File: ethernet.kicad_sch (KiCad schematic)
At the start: 39 parts, among them J1001 7499010121A, U1001 LAN8742A-CZ-TR, U1002 USBLC6-4SC6

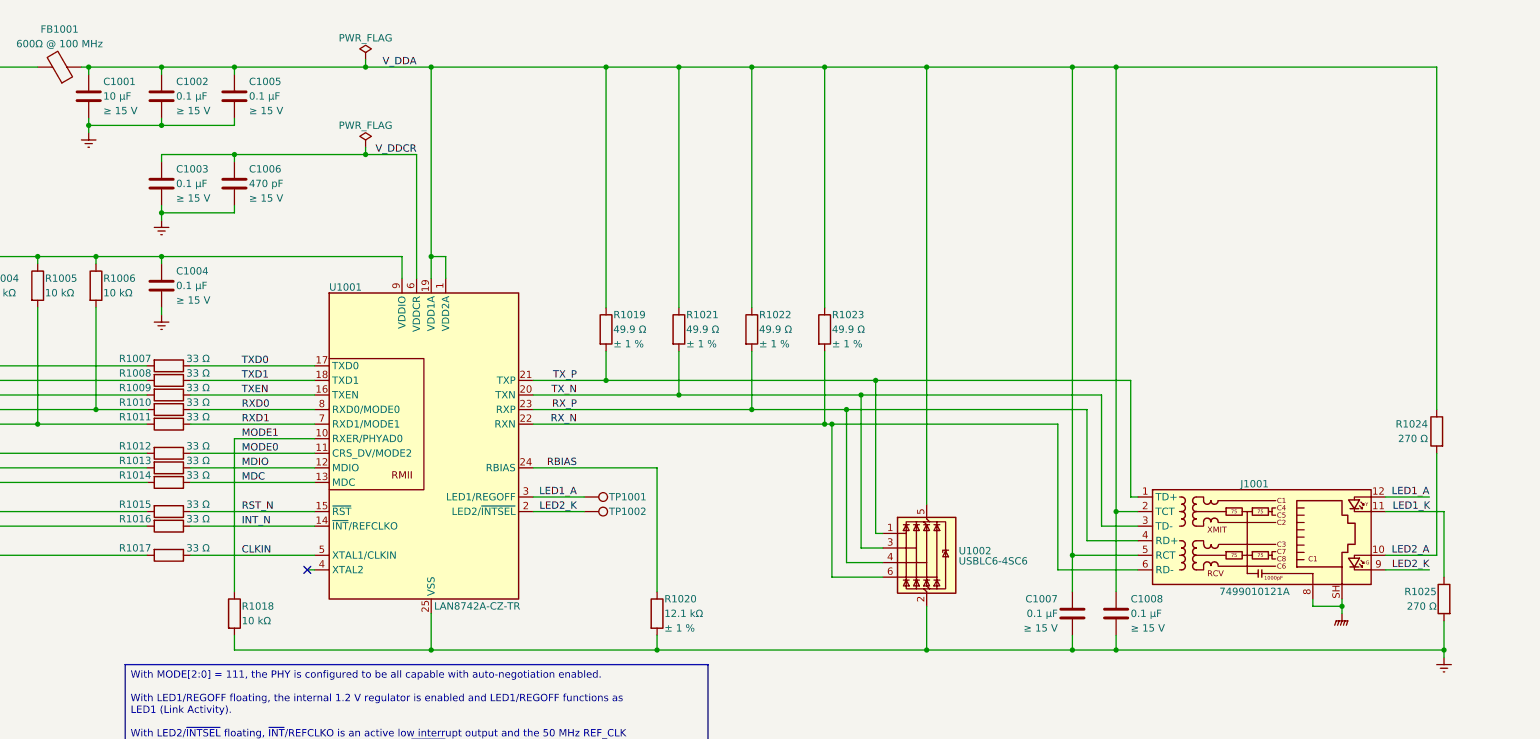
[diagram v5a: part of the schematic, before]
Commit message: Fix component values
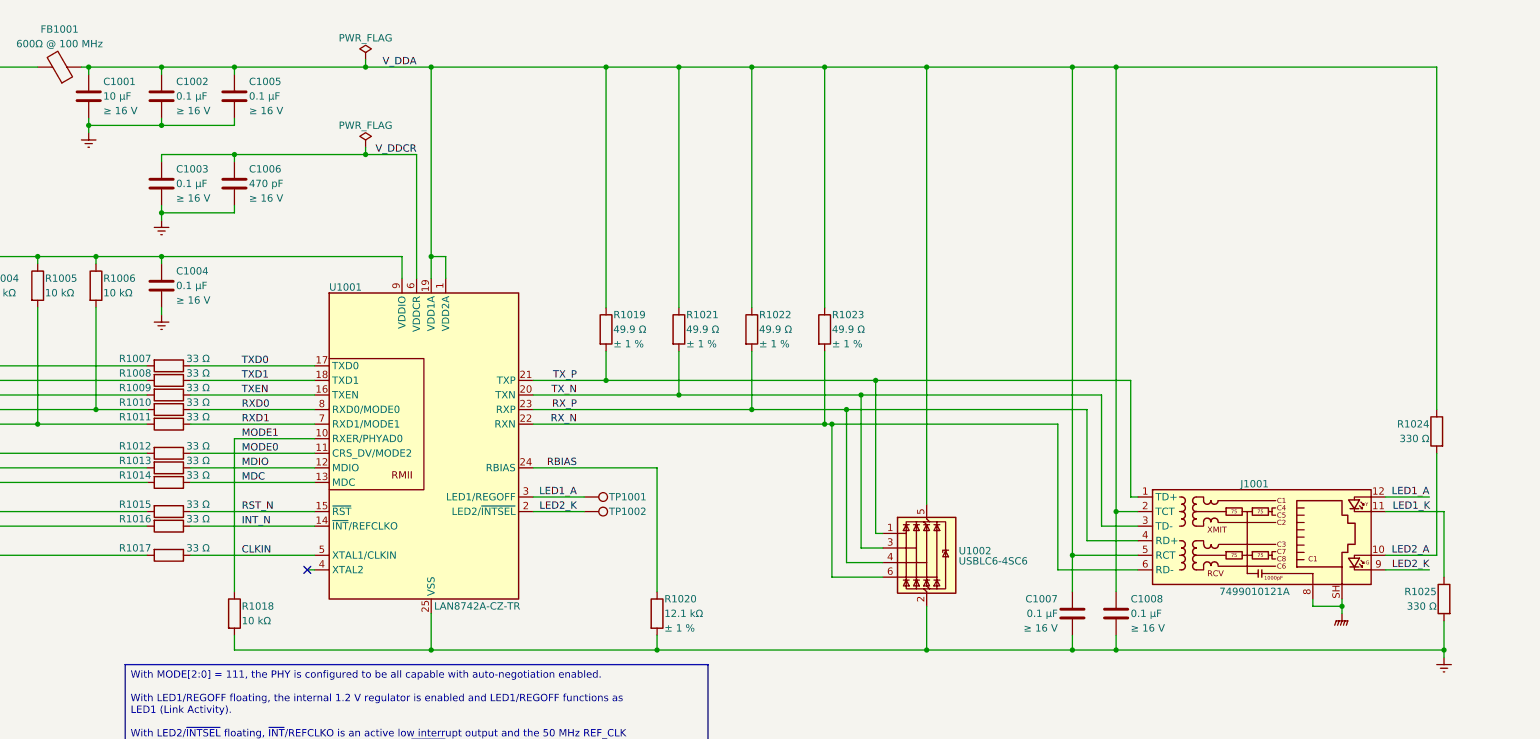
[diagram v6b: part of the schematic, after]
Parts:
- C1001, C1002, C1003, C1004, C1005, C1006, C1007, C1008: Voltage rating ≥ 15 V -> ≥ 16 V
- R1024, R1025: value 270 Ω -> 330 Ω; MPN (none) -> 560112110019; Manufacturer (none) -> Würth Elektronik
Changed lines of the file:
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@@
 			)
 		)
-		(property "Voltage rating" "≥ 15 V"
+		(property "Voltage rating" "≥ 16 V"
 			(at 135.89 140.9701 0)
 			(effects
@@
 			)
 		)
-		(property "Voltage rating" "≥ 15 V"
+		(property "Voltage rating" "≥ 16 V"
 			(at 289.56 215.9001 0)
 			(effects
@@
 			)
 		)
-		(property "Voltage rating" "≥ 15 V"
+		(property "Voltage rating" "≥ 16 V"
 			(at 148.59 125.7301 0)
 			(effects
@@
 	)
 	(symbol
-		(lib_id "Device:R")
-		(at 355.6 181.61 0)
-		(mirror y)
-		(unit 1)
-		(exclude_from_sim no)
-		(in_bom yes)
-		(on_board yes)
-		(dnp no)
-		(property "Reference" "R1024"
-			(at 354.076 180.34 0)
-			(effects
-				(font
-					(size 1.27 1.27)
-				)
-				(justify left)
-			)
-		)
-		(property "Value" "270 Ω"
-			(at 354.076 182.88 0)
-			(effects
-				(font
-					(size 1.27 1.27)
-				)
-				(justify left)
-			)
-		)
-		(property "Footprint" "perfect_footprints:R_0402_1005Metric"
-			(at 357.378 181.61 90)
-			(effects
-				(font
-					(size 1.27 1.27)
-				)
-				(hide yes)
-			)
-		)
-		(property "Datasheet" ""
-			(at 355.6 181.61 0)
-			(effects
-				(font
-					(size 1.27 1.27)
-				)
-				(hide yes)
-			)
-		)
-		(property "Description" "Resistor"
-			(at 355.6 181.61 0)
-			(effects
-				(font
-					(size 1.27 1.27)
-				)
-				(hide yes)
-			)
-		)
-		(property "MPN" ""
-			(at 355.6 181.61 0)
-			(effects
-				(font
-					(size 1.27 1.27)
-				)
-				(hide yes)
-			)
-		)
-		(property "Manufacturer" ""
-			(at 355.6 181.61 0)
-			(effects
-				(font
-					(size 1.27 1.27)
-				)
-				(hide yes)
-			)
-		)
-		(pin "2"
-		)
-		(pin "1"
-		)
-		(instances
-			(project "linux-sbc"
-				(path "/fa11a02f-8043-4153-ab69-88d766503017/9ca4e50e-b0f6-43cd-b87d-1fd05ae8a1fe"
-					(reference "R1024")
-					(unit 1)
-				)
-			)
-		)
-	)
-	(symbol
 		(lib_id "Power_Protection:USBLC6-4SC6")
 		(at 266.7 201.93 0)
@@
 			)
 		)
-		(property "Voltage rating" "≥ 15 V"
+		(property "Voltage rating" "≥ 16 V"
 			(at 123.19 125.7301 0)
 			(effects
@@
 			)
 		)
-		(property "Voltage rating" "≥ 15 V"
+		(property "Voltage rating" "≥ 16 V"
 			(at 135.89 158.7501 0)
 			(effects
@@
 			)
 		)
-		(property "Voltage rating" "≥ 15 V"
+		(property "Voltage rating" "≥ 16 V"
 			(at 148.59 140.9701 0)
 			(effects
@@
 	)
 	(symbol
+		(lib_id "Device:R")
+		(at 356.87 210.82 0)
+		(mirror y)
+		(unit 1)
+		(exclude_from_sim no)
+		(in_bom yes)
+		(on_board yes)
+		(dnp no)
+		(property "Reference" "R1025"
+			(at 355.6 209.55 0)
+			(effects
+				(font
+					(size 1.27 1.27)
+				)
+				(justify left)
+			)
+		)
+		(property "Value" "330 Ω"
+			(at 355.6 212.09 0)
+			(effects
+				(font
+					(size 1.27 1.27)
+				)
+				(justify left)
+			)
+		)
+		(property "Footprint" "perfect_footprints:R_0402_1005Metric"
+			(at 358.648 210.82 90)
+			(effects
+				(font
+					(size 1.27 1.27)
+				)
+				(hide yes)
+			)
+		)
+		(property "Datasheet" "https://www.we-online.com/components/products/datasheet/560112110019.pdf"
+			(at 356.87 210.82 0)
+			(effects
+				(font
+					(size 1.27 1.27)
+				)
+				(hide yes)
+			)
+		)
+		(property "Description" "Resistor"
+			(at 356.87 210.82 0)
+			(effects
+				(font
+					(size 1.27 1.27)
+				)
+				(hide yes)
+			)
+		)
+		(property "MPN" "560112110019"
+			(at 356.87 210.82 0)
+			(effects
+				(font
+					(size 1.27 1.27)
+				)
+				(hide yes)
+			)
+		)
+		(property "Manufacturer" "Würth Elektronik"
+			(at 356.87 210.82 0)
+			(effects
+				(font
+					(size 1.27 1.27)
+				)
+				(hide yes)
+			)
+		)
+		(pin "2"
+		)
+		(pin "1"
+		)
+		(instances
+			(project "linux-sbc"
+				(path "/fa11a02f-8043-4153-ab69-88d766503017/9ca4e50e-b0f6-43cd-b87d-1fd05ae8a1fe"
+					(reference "R1025")
+					(unit 1)
+				)
+			)
+		)
+	)
+	(symbol
 		(lib_id "Interface_Ethernet:LAN8742A")
 		(at 180.34 185.42 0)
@@
 	)
 	(symbol
-		(lib_id "Device:C")
-		(at 133.35 123.19 0)
+		(lib_id "Device:R")
+		(at 355.6 181.61 0)
+		(mirror y)
 		(unit 1)
 		(exclude_from_sim no)
@@
 		(on_board yes)
 		(dnp no)
-		(property "Reference" "C1002"
-			(at 135.89 120.65 0)
+		(property "Reference" "R1024"
+			(at 354.33 180.34 0)
 			(effects
 				(font
@@
 			)
 		)
-		(property "Value" "0.1 µF"
-			(at 135.89 123.19 0)
+		(property "Value" "330 Ω"
+			(at 354.33 182.88 0)
 			(effects
 				(font
@@
 			)
 		)
-		(property "Footprint" ""
-			(at 134.3152 127 0)
+		(property "Footprint" "perfect_footprints:R_0402_1005Metric"
+			(at 357.378 181.61 90)
 			(effects
 				(font
@@
 			)
 		)
-		(property "Datasheet" ""
-			(at 133.35 123.19 0)
+		(property "Datasheet" "https://www.we-online.com/components/products/datasheet/560112110019.pdf"
+			(at 355.6 181.61 0)
 			(effects
 				(font
@@
 			)
 		)
-		(property "Description" ""
-			(at 133.35 123.19 0)
+		(property "Description" "Resistor"
+			(at 355.6 181.61 0)
 			(effects
 				(font
@@
 			)
 		)
-		(property "MPN" ""
-			(at 133.35 123.19 0)
+		(property "MPN" "560112110019"
+			(at 355.6 181.61 0)
 			(effects
 				(font
@@
 			)
 		)
-		(property "Manufacturer" ""
-			(at 133.35 123.19 0)
+		(property "Manufacturer" "Würth Elektronik"
+			(at 355.6 181.61 0)
 			(effects
 				(font
@@
 			)
 		)
-		(property "Voltage rating" "≥ 15 V"
-			(at 135.89 125.7301 0)
-			(effects
-				(font
-					(size 1.27 1.27)
-				)
-				(justify left)
-			)
-		)
 		(pin "2"
 		)
@@
 			(project "linux-sbc"
 				(path "/fa11a02f-8043-4153-ab69-88d766503017/9ca4e50e-b0f6-43cd-b87d-1fd05ae8a1fe"
-					(reference "C1002")
+					(reference "R1024")
 					(unit 1)
 				)
@@
 	)
 	(symbol
-		(lib_id "Device:R")
-		(at 356.87 210.82 0)
-		(mirror y)
+		(lib_id "Device:C")
+		(at 133.35 123.19 0)
 		(unit 1)
 		(exclude_from_sim no)
@@
 		(on_board yes)
 		(dnp no)
-		(property "Reference" "R1025"
-			(at 355.6 209.55 0)
+		(property "Reference" "C1002"
+			(at 135.89 120.65 0)
 			(effects
 				(font
@@
 			)
 		)
-		(property "Value" "270 Ω"
-			(at 355.6 212.09 0)
+		(property "Value" "0.1 µF"
+			(at 135.89 123.19 0)
 			(effects
 				(font
@@
 			)
 		)
-		(property "Footprint" "perfect_footprints:R_0402_1005Metric"
-			(at 358.648 210.82 90)
+		(property "Footprint" ""
+			(at 134.3152 127 0)
 			(effects
 				(font
@@
 		)
 		(property "Datasheet" ""
-			(at 356.87 210.82 0)
+			(at 133.35 123.19 0)
 			(effects
 				(font
@@
 			)
 		)
-		(property "Description" "Resistor"
-			(at 356.87 210.82 0)
+		(property "Description" ""
+			(at 133.35 123.19 0)
 			(effects
 				(font
@@
 		)
 		(property "MPN" ""
-			(at 356.87 210.82 0)
+			(at 133.35 123.19 0)
 			(effects
 				(font
@@
 		)
 		(property "Manufacturer" ""
-			(at 356.87 210.82 0)
+			(at 133.35 123.19 0)
 			(effects
 				(font
@@
 			)
 		)
+		(property "Voltage rating" "≥ 16 V"
+			(at 135.89 125.7301 0)
+			(effects
+				(font
+					(size 1.27 1.27)
+				)
+				(justify left)
+			)
+		)
 		(pin "2"
 		)
@@
 			(project "linux-sbc"
 				(path "/fa11a02f-8043-4153-ab69-88d766503017/9ca4e50e-b0f6-43cd-b87d-1fd05ae8a1fe"
-					(reference "R1025")
+					(reference "C1002")
 					(unit 1)
 				)
@@
 			)
 		)
-		(property "Voltage rating" "≥ 15 V"
+		(property "Voltage rating" "≥ 16 V"
 			(at 302.26 215.9001 0)
 			(effects

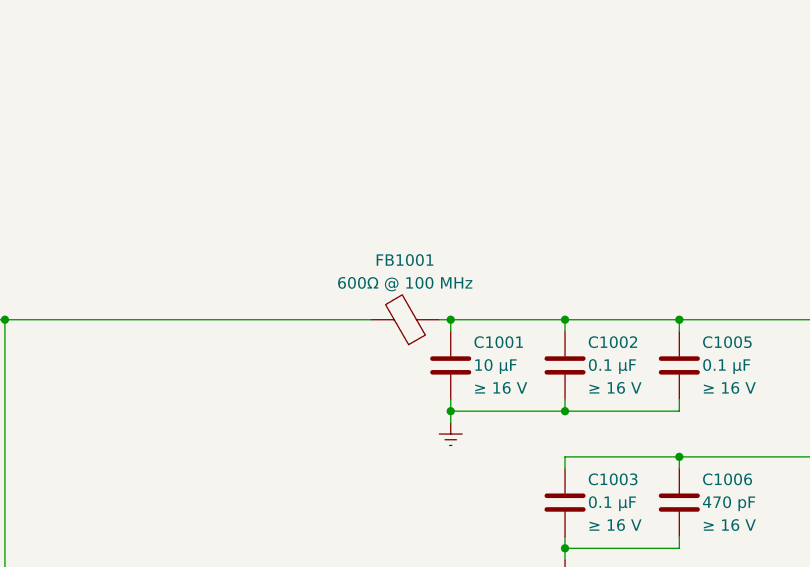
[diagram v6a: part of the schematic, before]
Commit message: Refactor schematics
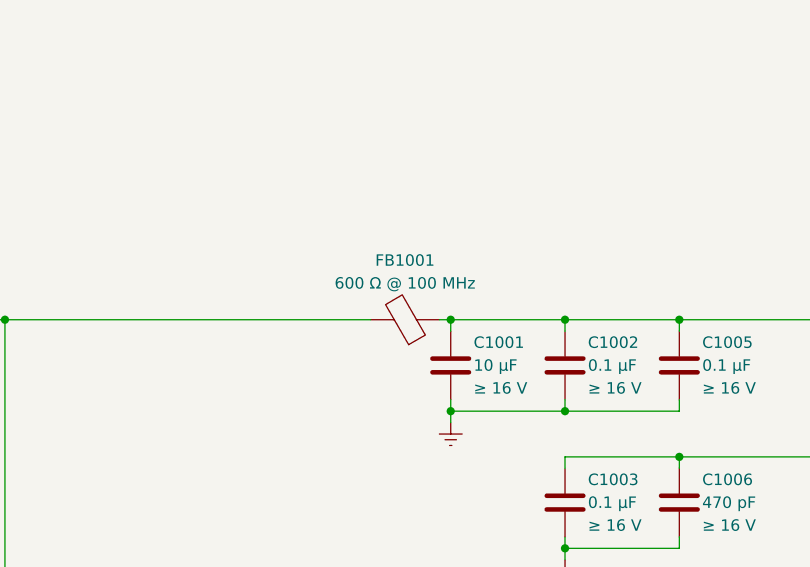
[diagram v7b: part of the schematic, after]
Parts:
- FB1001: value 600Ω @ 100 MHz -> 600 Ω @ 100 MHz
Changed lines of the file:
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@@
 			(justify right bottom)
 		)
-		(property "Netclass" "ETH_PAIR"
+		(property "Netclass" "ETH"
 			(at 216.5985 184.15 0)
 			(effects
@@
 			)
 		)
-		(property "Value" "600Ω @ 100 MHz"
+		(property "Value" "600 Ω @ 100 MHz"
 			(at 115.57 114.808 90)
 			(effects

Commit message: Clean-up schematics
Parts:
- R1007, R1008, R1009, R1013, R1014, R1015, R1017: value 33 Ω -> 0 Ω
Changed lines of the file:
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@@
 			)
 		)
-		(property "Value" "33 Ω"
+		(property "Value" "0 Ω"
 			(at 137.668 172.212 90)
 			(effects
@@
 			)
 		)
-		(property "Value" "33 Ω"
+		(property "Value" "0 Ω"
 			(at 137.668 174.752 90)
 			(effects
@@
 			)
 		)
-		(property "Value" "33 Ω"
+		(property "Value" "0 Ω"
 			(at 137.668 189.992 90)
 			(effects
@@
 			)
 		)
-		(property "Value" "33 Ω"
+		(property "Value" "0 Ω"
 			(at 137.668 169.672 90)
 			(effects
@@
 			)
 		)
-		(property "Value" "33 Ω"
+		(property "Value" "0 Ω"
 			(at 137.668 202.692 90)
 			(effects
@@
 			)
 		)
-		(property "Value" "33 Ω"
+		(property "Value" "0 Ω"
 			(at 137.668 187.452 90)
 			(effects
@@
 			)
 		)
-		(property "Value" "33 Ω"
+		(property "Value" "0 Ω"
 			(at 137.668 195.072 90)
 			(effects
